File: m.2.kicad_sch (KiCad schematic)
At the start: 4 parts, among them CN6 DF40C-20DP-0.4V, J9 Bus_M.2_Socket_B

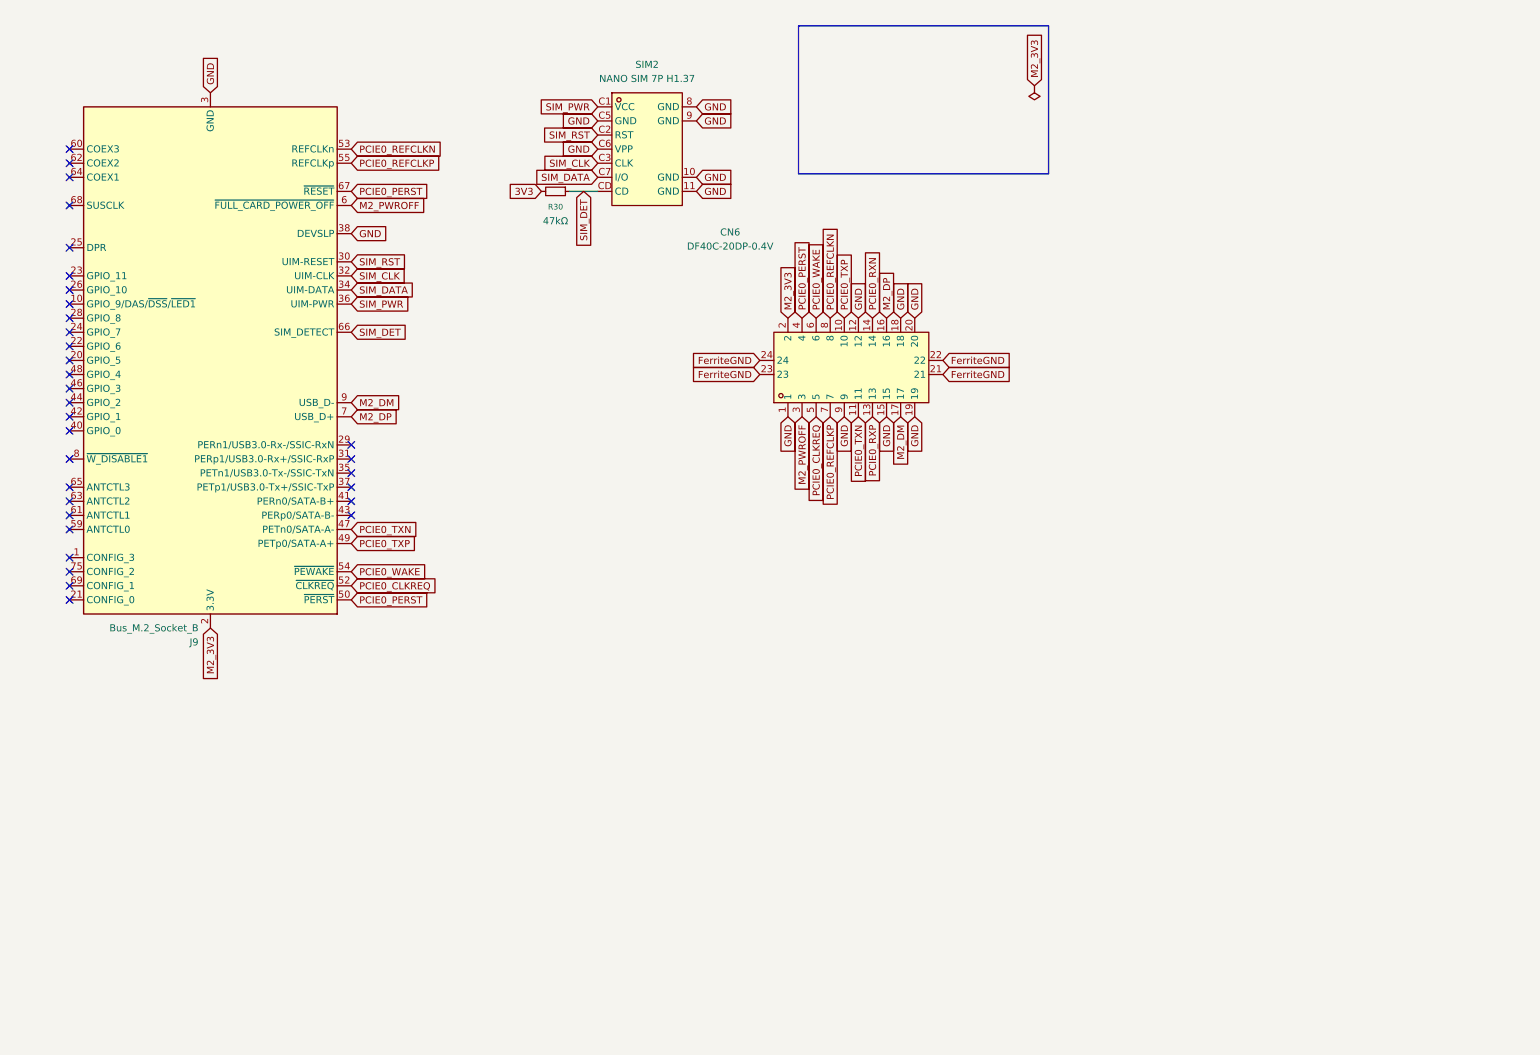
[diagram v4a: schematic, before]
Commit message: finished rf sense and io board closure, added audio system with pcm and three spdt switches, made changes tp lte module, added ldo and sd/sim slot, updated m.2/audio schematics, added new mic msop qfn sot footprints, and added a protection system for non EM06-A Cards
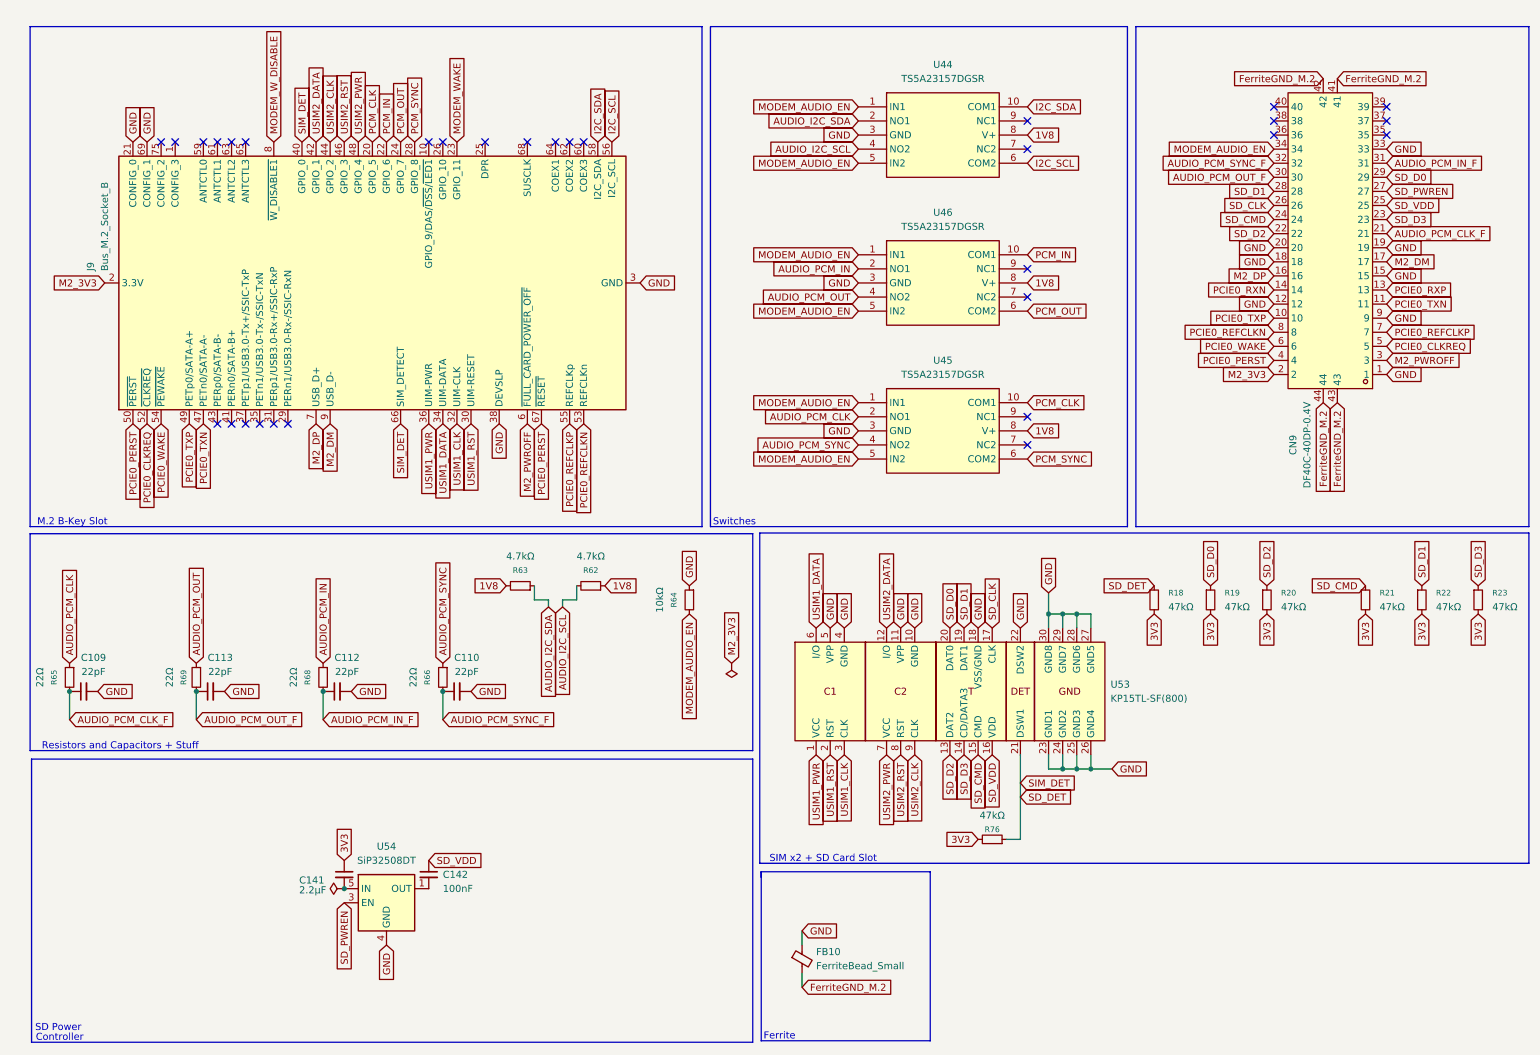
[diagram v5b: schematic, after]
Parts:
- removed CN6: DF40C-20DP-0.4V, slate113:CONN-SMD_20P-P0.40_HRS_DF40TC-20DP-0.4V, symbol slate113:DF40C-20DP-0.4V
- removed R30: 47kΩ, symbol Device:R_Small
- removed SIM2: NANO SIM 7P H1.37, slate113:SIM-SMD_NANO-SIM-7P-H1.37, symbol slate113:NANOSIM7PH1.37
- added C109, C110, C112, C113: 22pF, symbol Device:C_Small
- added C141: 2.2µF, symbol Device:C_Small
- added C142: 100nF, symbol Device:C_Small
- added CN9: DF40C-40DP-0.4V, slate113:CONN-SMD_DF40C-40DP-0.4V, symbol slate113:DF40C-40DP-0.4V
- added FB10: FerriteBead_Small, symbol Device:FerriteBead_Small
- added R18, R19, R20, R21, R22, R23, R76: 47kΩ, symbol Device:R_Small
- added R62, R63: 4.7kΩ, symbol Device:R_Small
- added R64: 10kΩ, symbol Device:R_Small
- added R65, R66, R68, R69: 22Ω, symbol Device:R_Small
- added U44, U45, U46: TS5A23157DGSR, slate113:MSOP-10_L3.0-W3.0-P0.50-LS5.0-BL, symbol slate113:TS5A23157DGSR
- added U53: KP15TL-SF(800), symbol slate113:KP15TL-SF(800)
- added U54: SiP32508DT, Package_TO_SOT_SMD:TSOT-23-6, symbol Power_Management:SiP32508DT
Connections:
- net SIM_DET is gone; now on net SD_DET: J9.66 (SIM_DETECT)
- net 3V3: now also C141.1, R18.2, R19.2, R20.2, R21.2, R22.2, R23.2, R76.2
- net GND: now also J9.21 (CONFIG_0), J9.69 (CONFIG_1), C109.2, C110.2, C112.2, C113.2, CN9.1, CN9.12, CN9.15, CN9.18, CN9.19, CN9.20, CN9.33, CN9.9, FB10.1, R64.1, U44.3 (GND), U45.3 (GND), U46.3 (GND), U53.10 (GND), U53.11 (VPP), U53.18 (VSS/GND), U53.22 (DSW2), U53.23 (GND1), U53.24 (GND2), U53.25 (GND3), U53.26 (GND4), U53.27 (GND5), U53.28 (GND6), U53.29 (GND7), U53.30 (GND8), U53.4 (GND), U53.5 (VPP), U54.4 (GND)
- net M2_3V3: now also CN9.2
- net M2_DM: now also CN9.17
- net M2_DP: now also CN9.16
- net M2_PWROFF: now also CN9.3
- net PCIE0_CLKREQ: now also CN9.5
- net PCIE0_PERST: now also CN9.4
- net PCIE0_REFCLKN: now also CN9.8
- net PCIE0_REFCLKP: now also CN9.7
- net PCIE0_RXN: now also CN9.14
- net PCIE0_RXP: now also CN9.13
- net PCIE0_TXN: now also CN9.11
- net PCIE0_TXP: now also CN9.10
- net PCIE0_WAKE: now also CN9.6
- net PCM_CLK: now reaches J9.20 (GPIO_5)
- net PCM_CLK: now also U45.10 (COM1)
- net PCM_IN: now reaches J9.22 (GPIO_6)
- net PCM_IN: now also U46.10 (COM1)
- net MODEM_WAKE: now reaches J9.23 (GPIO_11)
- net PCM_OUT: now reaches J9.24 (GPIO_7)
- net PCM_OUT: now also U46.6 (COM2)
- net PCM_SYNC: now reaches J9.28 (GPIO_8)
- net PCM_SYNC: now also U45.6 (COM2)
- net SD_DET: now reaches J9.40 (GPIO_0)
- net SD_DET: now also R18.1, R76.1, U53.21 (DSW1)
- net USIM2_DATA: now reaches J9.42 (GPIO_1)
- net USIM2_DATA: now also U53.12 (I/O)
- net USIM2_CLK: now reaches J9.44 (GPIO_2)
- net USIM2_CLK: now also U53.9 (CLK)
- net USIM2_RST: now reaches J9.46 (GPIO_3)
- net USIM2_RST: now also U53.8 (RST)
- net USIM2_PWR: now reaches J9.48 (GPIO_4)
- net USIM2_PWR: now also U53.7 (VCC)
- net I2C_SCL: now reaches J9.56 (I2C_SCL)
- net I2C_SCL: now also U44.6 (COM2)
- net I2C_SDA: now reaches J9.58 (I2C_SDA)
- net I2C_SDA: now also U44.10 (COM1)
- net MODEM_W_DISABLE: now reaches J9.8 (~{W_DISABLE1})
- net SIM_CLK renamed USIM1_CLK
- net USIM1_CLK: now also U53.3 (CLK)
- net SIM_DATA renamed USIM1_DATA
- net USIM1_DATA: now also U53.6 (I/O)
- net SIM_PWR renamed USIM1_PWR
- net USIM1_PWR: now also U53.1 (VCC)
- net SIM_RST renamed USIM1_RST
- net USIM1_RST: now also U53.2 (RST)
- new net: C141.2, U54.5 (IN), U54.6 (IN)
- new net: C142.2, U54.1 (OUT), U54.2 (OUT)
- new net 1V8: R62.1, R63.2, U44.8 (V+), U45.8 (V+), U46.8 (V+)
- new net AUDIO_I2C_SCL: R62.2, U44.4 (NO2)
- new net AUDIO_I2C_SDA: R63.1, U44.2 (NO1)
- new net AUDIO_PCM_CLK: R65.1, U45.2 (NO1)
- new net AUDIO_PCM_CLK_F: C109.1, CN9.21, R65.2
- new net AUDIO_PCM_IN: R68.1, U46.2 (NO1)
- new net AUDIO_PCM_IN_F: C112.1, CN9.31, R68.2
- new net AUDIO_PCM_OUT: R69.1, U46.4 (NO2)
- new net AUDIO_PCM_OUT_F: C113.1, CN9.30, R69.2
- new net AUDIO_PCM_SYNC: R66.1, U45.4 (NO2)
- new net AUDIO_PCM_SYNC_F: C110.1, CN9.32, R66.2
- new net FerriteGND_M.2: CN9.41, CN9.42, CN9.43, CN9.44, FB10.2
- new net MODEM_AUDIO_EN: CN9.34, R64.2, U44.1 (IN1), U44.5 (IN2), U45.1 (IN1), U45.5 (IN2), U46.1 (IN1), U46.5 (IN2)
- new net SD_CLK: CN9.26, U53.17 (CLK)
- new net SD_CMD: CN9.24, R21.1, U53.15 (CMD)
- new net SD_D0: CN9.29, R19.1, U53.20 (DAT0)
- new net SD_D1: CN9.28, R22.1, U53.19 (DAT1)
- new net SD_D2: CN9.22, R20.1, U53.13 (DAT2)
- new net SD_D3: CN9.23, R23.1, U53.14 (CD/DATA3)
- new net SD_PWREN: CN9.27, U54.3 (EN)
- new net SD_VDD: C142.1, CN9.25, U53.16 (VDD)
- no-connect marks 32 -> 31
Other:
- note added: "Controller"
- note added: "Ferrite"
- note added: "M.2 B-Key Slot"
- note added: "Resistors and Capacitors + Stuff"
- note added: "SD Power"
- note added: "SIM x2 + SD Card Slot"
- note added: "Switches"

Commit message: finished slateconnect i2c gpio expander, completed led status bar schematic, fixed all drc errors, started assigning footprints and started bom
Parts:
- C110, C113: footprint (none) -> Capacitor_SMD:C_0603_1608Metric; MPN (none) -> CL10C220JB8NNNC; Manufacturer (none) -> Samsung Electro-Mechanics
- C141: footprint (none) -> Capacitor_SMD:C_0603_1608Metric; MPN (none) -> CL10B225KA8NNNC; Manufacturer (none) -> Samsung Electro-Mechanics
- C142: footprint (none) -> Capacitor_SMD:C_0603_1608Metric; MPN (none) -> CL10B104KB8NNNC; Manufacturer (none) -> Samsung Electro-Mechanics
- J9: MPN (none) -> Bus_M.2_Socket_B; Manufacturer (none) -> LCSC
- R18, R22: footprint (none) -> Resistor_SMD:R_0603_1608Metric; MPN (none) -> RC0603FR-0747KL; Manufacturer (none) -> Yageo
- R62, R63: footprint (none) -> Resistor_SMD:R_0603_1608Metric; MPN (none) -> RC0603FR-074K7L; Manufacturer (none) -> Yageo
- R64: footprint (none) -> Resistor_SMD:R_0603_1608Metric; MPN (none) -> RC0603FR-0710KL; Manufacturer (none) -> Yageo
- R66, R68, R69: footprint (none) -> Resistor_SMD:R_0603_1608Metric; MPN (none) -> RC0603FR-0722RL; Manufacturer (none) -> Yageo
- U53: MPN (none) -> KP15TL-SF(800); Manufacturer (none) -> LCSC
- U54: MPN (none) -> SiP32508DT; Manufacturer (none) -> LCSC

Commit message: finished BOM, replaced discontinued parts, added missing footprints, updated schematics and libraries
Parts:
- added U64: TF PUSH, symbol slate113:TF-PUSH
- C109, C112: footprint (none) -> Capacitor_SMD:C_0402_1005Metric; LCSC Part (none) -> C1555; MPN (none) -> 0402CG220J500NT
- C110, C113: LCSC Part (none) -> C1555; MPN CL10C220JB8NNNC -> 0402CG220J500NT
- C141: LCSC Part (none) -> C23630; MPN CL10B225KA8NNNC -> CL10A225KO8NNNC
- C142: LCSC Part (none) -> C1591
- FB10: footprint (none) -> Inductor_SMD:L_0603_1608Metric; LCSC Part (none) -> C107335; MPN (none) -> MPZ1608S601ATA00; Manufacturer (none) -> TDK
- J9: DigiKey Part (none) -> MDT420B03001TR-ND; LCSC Part (none) -> C4885179; MPN Bus_M.2_Socket_B -> MDT420B03001; Manufacturer LCSC -> Amphenol ICC (FCI)
- R18, R22: LCSC Part (none) -> C105579
- R19, R20, R21, R23, R76: footprint (none) -> Resistor_SMD:R_0603_1608Metric; LCSC Part (none) -> C105579; MPN (none) -> RC0603FR-0747KL
- R62, R63: LCSC Part (none) -> C23162; MPN RC0603FR-074K7L -> 0603WAF4701T5E
- R64: LCSC Part (none) -> C25804; MPN RC0603FR-0710KL -> 0603WAF1002T5E
- R65: footprint (none) -> Resistor_SMD:R_0603_1608Metric; LCSC Part (none) -> C107701; MPN (none) -> RC0603FR-0722RL
- R66, R68, R69: LCSC Part (none) -> C107701
- U53: value KP15TL-SF(800) -> NANO SIM 7P 1.37H PUSH; symbol slate113:KP15TL-SF(800) -> slate113:NANO-SIM-7P-1.37H-PUSH; LCSC Part (none) -> C53207808; MPN KP15TL-SF(800) -> NANO SIM 7P 1.37H PUSH; Manufacturer LCSC -> JXTCONN
- U54: LCSC Part (none) -> C139515; MPN SiP32508DT -> SIP32508DT-T1-GE3
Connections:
- net GND: no longer U53.10 (GND), U53.11 (VPP), U53.18 (VSS/GND), U53.22 (DSW2), U53.23 (GND1), U53.24 (GND2), U53.25 (GND3), U53.26 (GND4), U53.27 (GND5), U53.28 (GND6), U53.29 (GND7), U53.30 (GND8), U53.4 (GND), U53.5 (VPP)
- net SD_CLK: no longer U53.17 (CLK)
- net SD_CMD: no longer U53.15 (CMD)
- net SD_D0: no longer U53.20 (DAT0)
- net SD_D1: no longer U53.19 (DAT1)
- net SD_D2: no longer U53.13 (DAT2)
- net SD_D3: no longer U53.14 (CD/DATA3)
- net SD_DET: no longer U53.21 (DSW1)
- net SD_VDD: no longer U53.16 (VDD)
- net USIM1_CLK: no longer U53.3 (CLK)
- net USIM1_DATA: no longer U53.6 (I/O)
- net USIM1_PWR: no longer U53.1 (VCC)
- net USIM1_RST: no longer U53.2 (RST)
- net USIM2_CLK: no longer U53.9 (CLK)
- net USIM2_DATA: no longer U53.12 (I/O)
- net USIM2_PWR: no longer U53.7 (VCC)
- net USIM2_RST: no longer U53.8 (RST)
